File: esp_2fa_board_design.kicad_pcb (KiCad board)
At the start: 2 copper layers, 0 parts

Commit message: Started layout of components. Fixed the Edge cut of PCB and rough location of components. Routing is yet to be done
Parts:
- added BT1: 3v, BU2032SM-BT-GTR:BU2032SMBTGTR, B.Cu at (108.7, 110.8)
- added Brd1: SSD1306, SSD1306:128x64OLED, F.Cu at (132.0, 92.7)
- added C3: 1uF, Capacitor_SMD:C_1206_3216Metric, F.Cu at (167.7, 91.2)
- added C4: 10uF, Capacitor_SMD:C_1206_3216Metric, F.Cu at (144.8, 97.5)
- added C5: 1uF, Capacitor_SMD:C_1206_3216Metric, F.Cu at (114.3, 118.8)
- added C6: 10uF, Capacitor_SMD:C_1206_3216Metric, F.Cu at (153.2, 114.4)
- added C7: 0.1uF, Capacitor_SMD:C_1206_3216Metric, F.Cu at (157.9, 117.6)
- added C8: 10uF, Capacitor_SMD:C_1206_3216Metric, F.Cu at (162.1, 114.4)
- added C9: 10uF, Capacitor_SMD:C_1206_3216Metric, F.Cu at (165.8, 114.4)
- added D2: LED, LED_SMD:LED_0603_1608Metric_Castellated, F.Cu at (149.5, 93.7)
- added D3: 1N5819, Diode_SMD:D_SOD-123, F.Cu at (162.0, 95.2)
- added IC1: TPS22919DCKR, TPS22919DCKR:SOT65P210X110-6N, F.Cu at (109.6, 119.5)
- added J1: Conn_01x06_Female, Connector_PinHeader_2.00mm:PinHeader_1x06_P2.00mm_Vertical, F.Cu at (119.6, 119.0)
- added J2: TYPE-C-31-M-17, TYPE-C-31-M-17:TYPEC31M17, F.Cu at (152.8, 84.4)
- added L1: 2.2 uH, CDRH104RNP-150NC:INDPM102100X400N, F.Cu at (157.2, 106.7)
- added Q1: DMP2305U-7, DMP2305U-7:SOT96P240X110-3N, F.Cu at (158.4, 94.8)
- added R1: 100, Resistor_SMD:R_0603_1608Metric, F.Cu at (161.9, 117.6)
- added R10: 100k, Resistor_SMD:R_0603_1608Metric, F.Cu at (168.0, 95.3)
- added R11: 5.1k, Resistor_SMD:R_0603_1608Metric, F.Cu at (149.1, 90.5)
- added R12: 5.1k, Resistor_SMD:R_0603_1608Metric, F.Cu at (156.4, 90.5)
- added R13: 10k, Resistor_SMD:R_0603_1608Metric, F.Cu at (155.6, 94.7)
- added R14: 10k, Resistor_SMD:R_0603_1608Metric, F.Cu at (119.8, 114.6)
- added R2: 4.7k, Resistor_SMD:R_0603_1608Metric, F.Cu at (105.6, 110.0)
- added R3: 4.7k, Resistor_SMD:R_0603_1608Metric, F.Cu at (105.6, 119.0)
- added R4: 10k, Resistor_SMD:R_0603_1608Metric, F.Cu at (119.8, 111.1)
- added R5: 10k, Resistor_SMD:R_0603_1608Metric, F.Cu at (161.5, 90.7)
- added R6: 10k, Resistor_SMD:R_0603_1608Metric, F.Cu at (134.2, 111.0)
- added R7: 4.7k, Resistor_SMD:R_0603_1608Metric, F.Cu at (149.3, 95.2)
- added R8: 1k, Resistor_SMD:R_0603_1608Metric, F.Cu at (146.9, 94.5)
- added R9: 100k, Resistor_SMD:R_0603_1608Metric, F.Cu at (166.0, 95.3)
- added REF**: OSHW-Logo_19x20mm_SilkScreen, Symbol:OSHW-Logo_19x20mm_SilkScreen, B.Cu at (125.9, 92.5)
- added REF**: KiCad-Logo2_5mm_SilkScreen, Symbol:KiCad-Logo2_5mm_SilkScreen, B.Cu at (141.3, 86.6)
- added SW1: SW_Push, Button_Switch_SMD:SW_Push_1P1T_NO_6x6mm_H9.5mm, F.Cu at (113.3, 112.8)
- added SW2: SW_Push, Button_Switch_SMD:SW_Push_1P1T_NO_6x6mm_H9.5mm, F.Cu at (127.0, 112.8)
- added SW3: BOOT, Button_Switch_SMD:SW_Push_1P1T_NO_6x6mm_H9.5mm, F.Cu at (140.3, 112.8)
- added SW4: RESET, Button_Switch_SMD:SW_Push_1P1T_NO_6x6mm_H9.5mm, F.Cu at (165.1, 85.2)
- added U1: ESP32-WROOM-32, RF_Module:ESP32-WROOM-32, F.Cu at (102.1, 95.9)
- added U2: DS3231M, Package_SO:SOIC-16W_7.5x10.3mm_P1.27mm, F.Cu at (97.7, 114.5)
- added U3: MCP73831-2-OT, Package_TO_SOT_SMD:SOT-23-5, F.Cu at (148.0, 97.9)
- added U4: TPS63001, Package_SON:Texas_DRC0010J_ThermalVias, F.Cu at (157.6, 114.3)
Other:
- board outline added: 82 x 45 mm

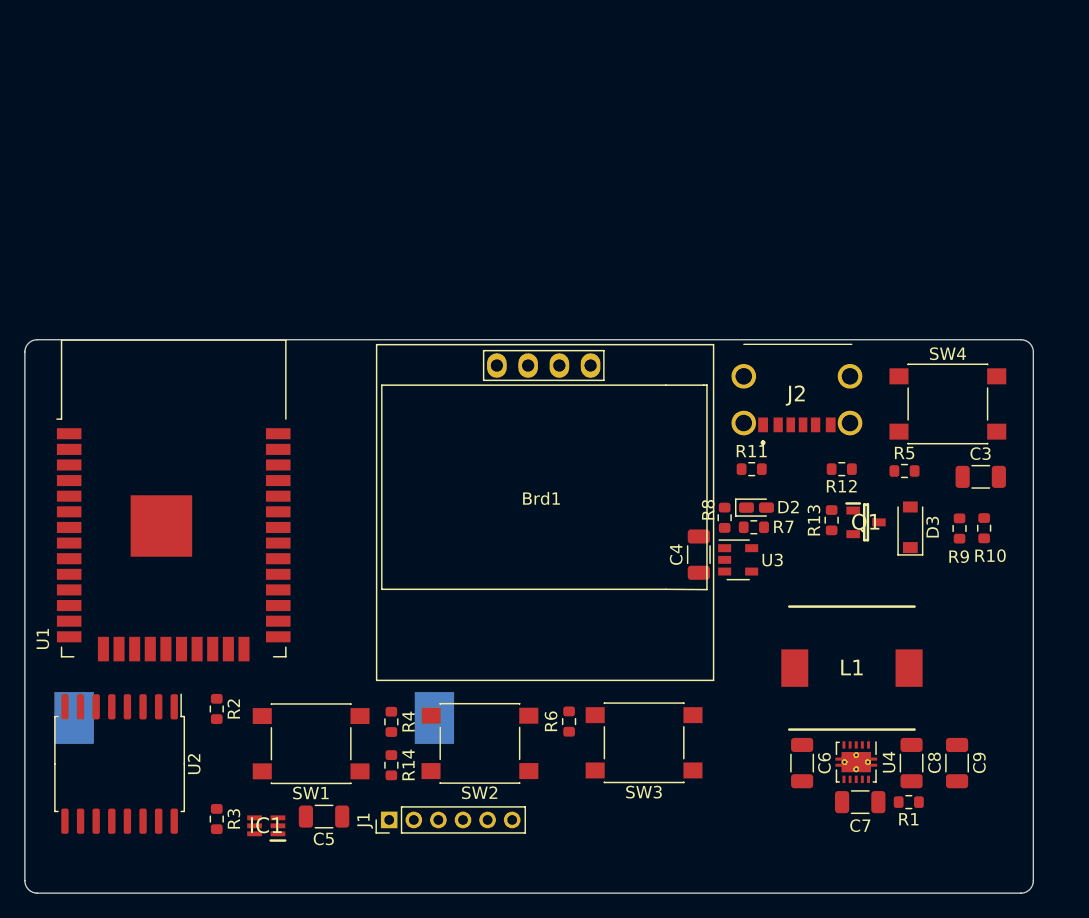
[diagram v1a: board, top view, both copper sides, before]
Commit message: Partially completed routing
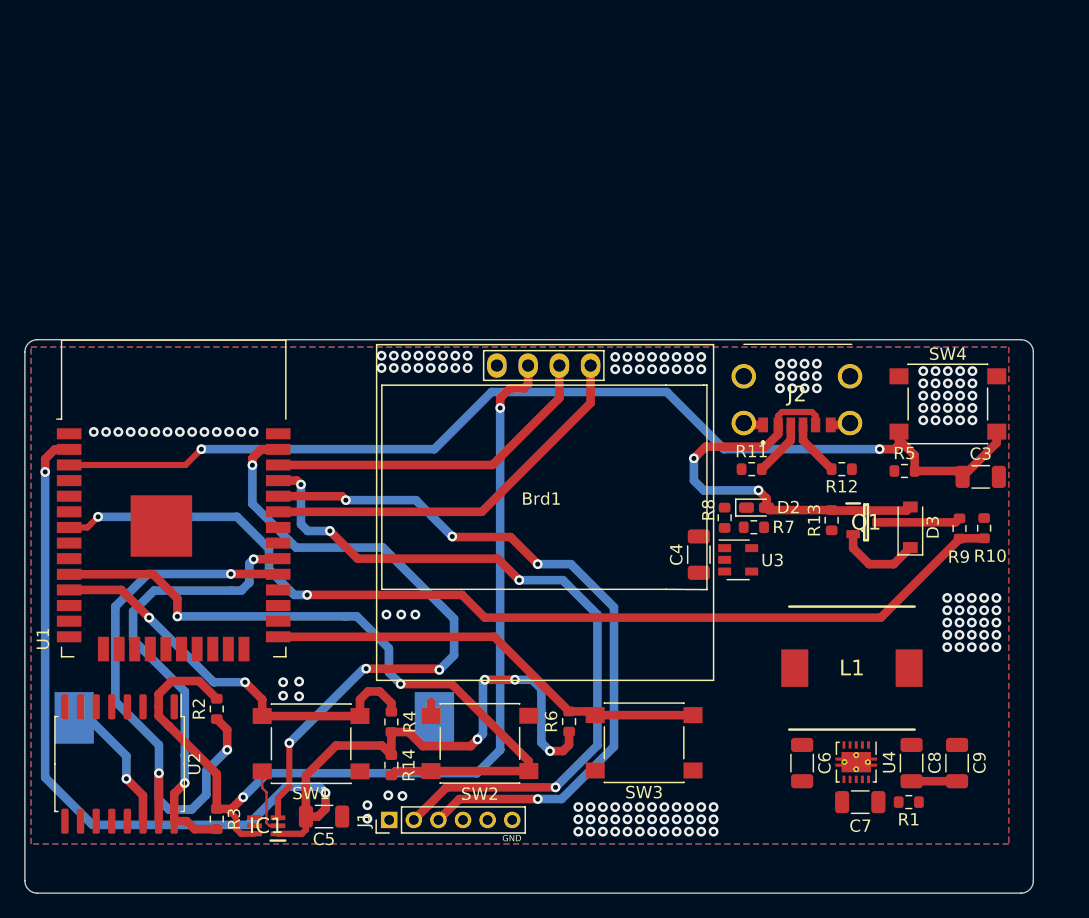
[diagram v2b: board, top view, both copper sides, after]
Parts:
- turned BT1 to 180 degrees
- turned R2 to 270 degrees
- turned R4 to 90 degrees
- turned SW2 to 0 degrees
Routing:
- net +3V3: track 0.00 -> 104.1 mm, vias 0 -> 6
- net /EN: track 0.00 -> 85.7 mm, vias 0 -> 2
- net /A1_7_BATT: track 0.00 -> 81.8 mm, vias 0 -> 2
- net /LOAD_SWITCH_VCC: track 0.00 -> 79.4 mm, vias 0 -> 2
- net /TX: track 0.00 -> 60.4 mm, vias 0 -> 4
- net /RX: track 0.00 -> 59.1 mm, vias 0 -> 4
- net /IO25: track 0.00 -> 57.8 mm, vias 0 -> 2
- net /IO23: track 0.00 -> 52.2 mm, vias 0 -> 4
- net /IO5_SDA: track 0.00 -> 47.3 mm, vias 0 -> 3
- net /IO18_SCL: track 0.00 -> 37.4 mm, vias 0 -> 2
- net /BOOT: track 0.00 -> 36.4 mm
- net VBUS: track 0.00 -> 34.2 mm, vias 0 -> 2
- net /IO26: track 0.00 -> 34.0 mm, vias 0 -> 2
- net /IO21_SDA: track 0.00 -> 32.1 mm
- net /IO22_SCL: track 0.00 -> 27.8 mm
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- added copper zone on B.Cu, net GND
- added copper zone on F.Cu, net GND
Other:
- net class Default: clearance 0.000254 -> 0.2; trace_width 0.000254 -> 0.2; via_dia 0.000762 -> 0.8; via_drill 0.000381 -> 0.4
- rule trace_clearance: 0.000254 -> 0.2
- board text added: "GND"

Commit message: Addede datasheets and partially completed routing
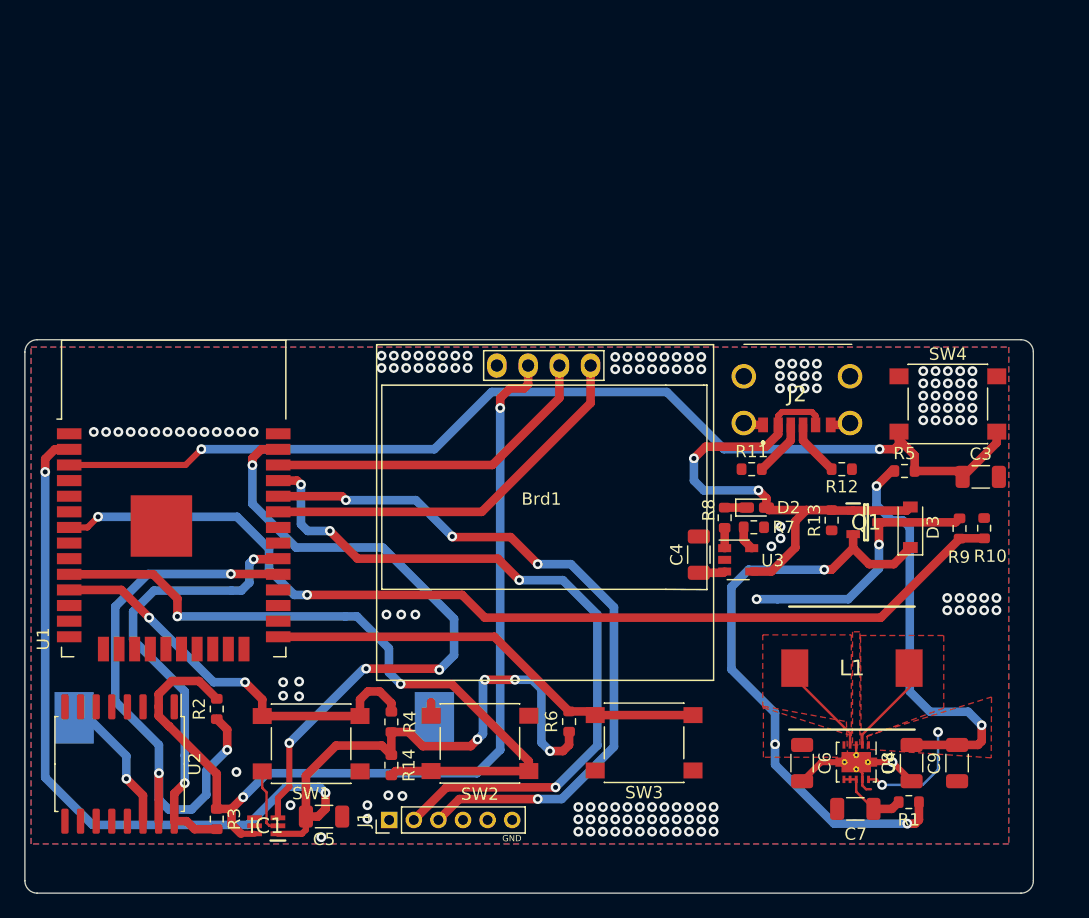
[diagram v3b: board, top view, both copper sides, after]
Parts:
- moved C7 0.68 mm to (157.5, 118.2), turned to 180 degrees
- turned C8 to 270 degrees
- turned C9 to 270 degrees
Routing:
- net /V_INPUT: track 6.89 -> 49.3 mm, vias 0 -> 3
- net +3V3: track 104.1 -> 144.2 mm, vias 6 -> 10
- net +BATT: track 6.68 -> 23.6 mm, vias 0 -> 2
- net GND: track 9.81 -> 21.4 mm, vias 155 -> 147
- net Net-(L1-Pad1): track 0.00 -> 8.11 mm
- net Net-(L1-Pad2): track 0.00 -> 7.82 mm
- net VBUS: track 34.2 -> 42.0 mm
- net Net-(C7-Pad1): track 0.00 -> 6.26 mm
- net Net-(R7-Pad1): track 0.00 -> 1.97 mm
- net Net-(D2-Pad1): track 0.00 -> 1.78 mm
- net Net-(R8-Pad1): track 0.00 -> 1.65 mm
- added copper zone on F.Cu, net +3V3
- added copper zone on F.Cu, net /V_INPUT
- added copper zone on F.Cu, net Net-(L1-Pad1)
- added copper zone on F.Cu, net Net-(L1-Pad2)

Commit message: Completed PCB routing
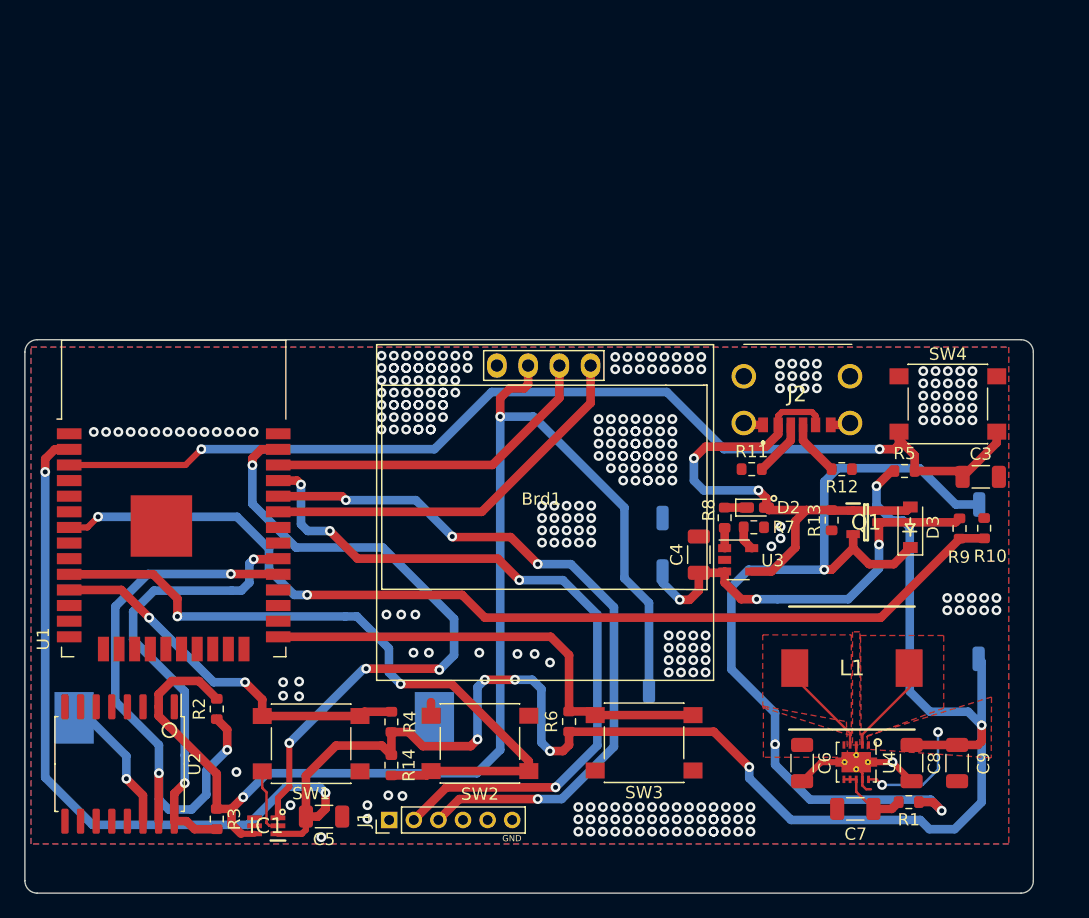
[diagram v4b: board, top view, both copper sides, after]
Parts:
- added +BATT: +BATT, Connector_Wire:SolderWirePad_1x01_SMD_1x2mm, B.Cu at (141.8, 98.8)
- added GND: GND, Connector_Wire:SolderWirePad_1x01_SMD_1x2mm, B.Cu at (141.8, 94.5)
- added TP1: 3V3, Connector_Wire:SolderWirePad_1x01_SMD_1x2mm, B.Cu at (167.6, 106.0)
- added TP4: LOAD_SWITCH, Connector_Wire:SolderWirePad_1x01_SMD_1x2mm, B.Cu at (140.8, 108.5)
- added TP5: V_INPUT, Connector_Wire:SolderWirePad_1x01_SMD_1x2mm, B.Cu at (167.6, 93.4)
- moved REF** 1.39 mm to (140.1, 87.2)
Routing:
- net +3V3: track 144.2 -> 194.2 mm, vias 10 -> 11
- net /LOAD_SWITCH_VCC: track 79.3 -> 108.2 mm
- net /V_INPUT: track 49.3 -> 72.7 mm
- net +BATT: track 23.6 -> 33.8 mm, vias 2 -> 3
- net /BOOT: track 36.4 -> 39.0 mm
- net /IO26: track 34.0 -> 31.4 mm
- net GND: vias 147 -> 289
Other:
- board text added: "Open Authenticator"
- board text added: "v1.2 Vedant Paranjape"

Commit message: Updated schematics according review feedback
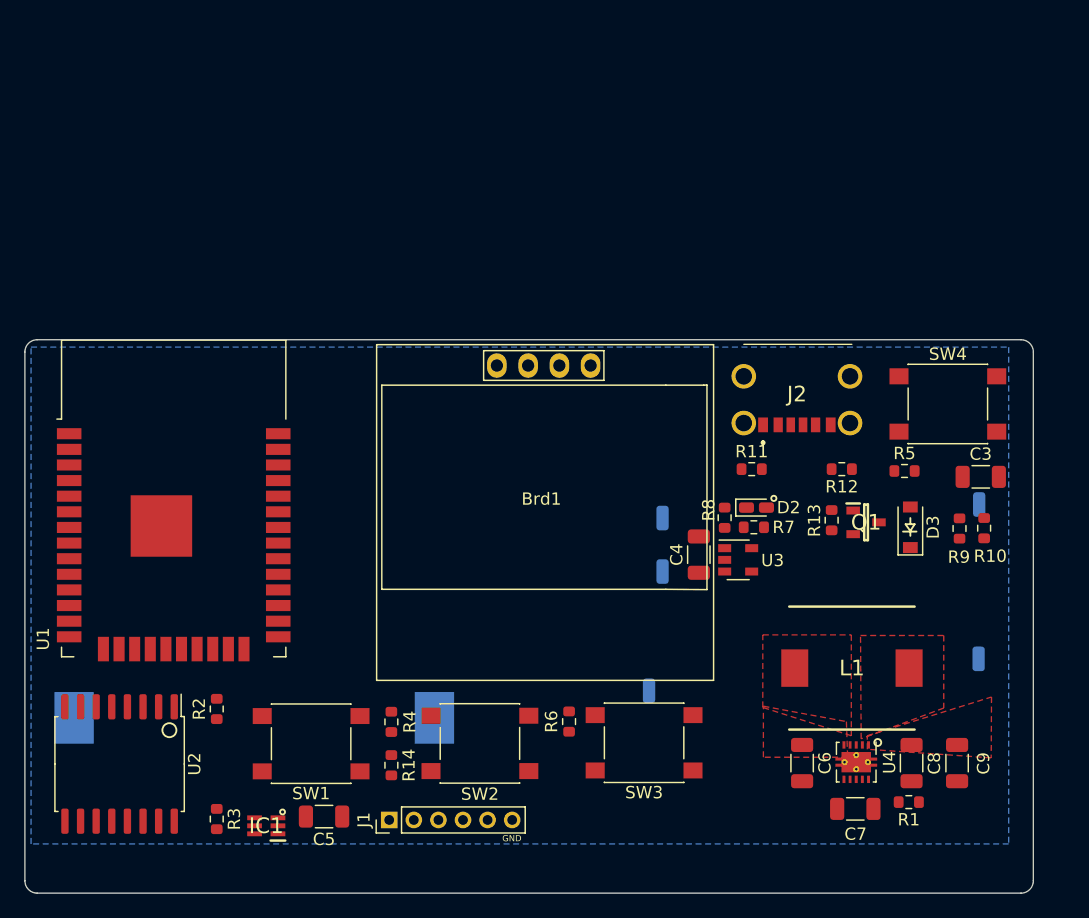
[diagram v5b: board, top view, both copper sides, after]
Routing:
- net +3V3: track 194.2 -> 0.00 mm, vias 11 -> 0
- net /LOAD_SWITCH_VCC: track 108.2 -> 0.00 mm, vias 2 -> 0
- net /EN: track 85.7 -> 0.00 mm, vias 2 -> 0
- net /A1_7_BATT: track 81.8 -> 0.00 mm, vias 2 -> 0
- net /V_INPUT: track 72.7 -> 0.00 mm, vias 3 -> 0
- net /TX: track 60.4 -> 0.00 mm, vias 4 -> 0
- net /RX: track 59.1 -> 0.00 mm, vias 4 -> 0
- net /IO25: track 57.8 -> 0.00 mm, vias 2 -> 0
- net /IO23: track 52.2 -> 0.00 mm, vias 4 -> 0
- net /IO5_SDA: track 47.3 -> 0.00 mm, vias 3 -> 0
- net VBUS: track 42.0 -> 0.00 mm, vias 2 -> 0
- net /BOOT: track 39.0 -> 0.00 mm
- net /IO18_SCL: track 37.4 -> 0.00 mm, vias 2 -> 0
- net +BATT: track 33.8 -> 0.00 mm, vias 3 -> 0
- net /IO21_SDA: track 32.1 -> 0.00 mm
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- removed copper zone on F.Cu, net GND

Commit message: Partially completed rerouting
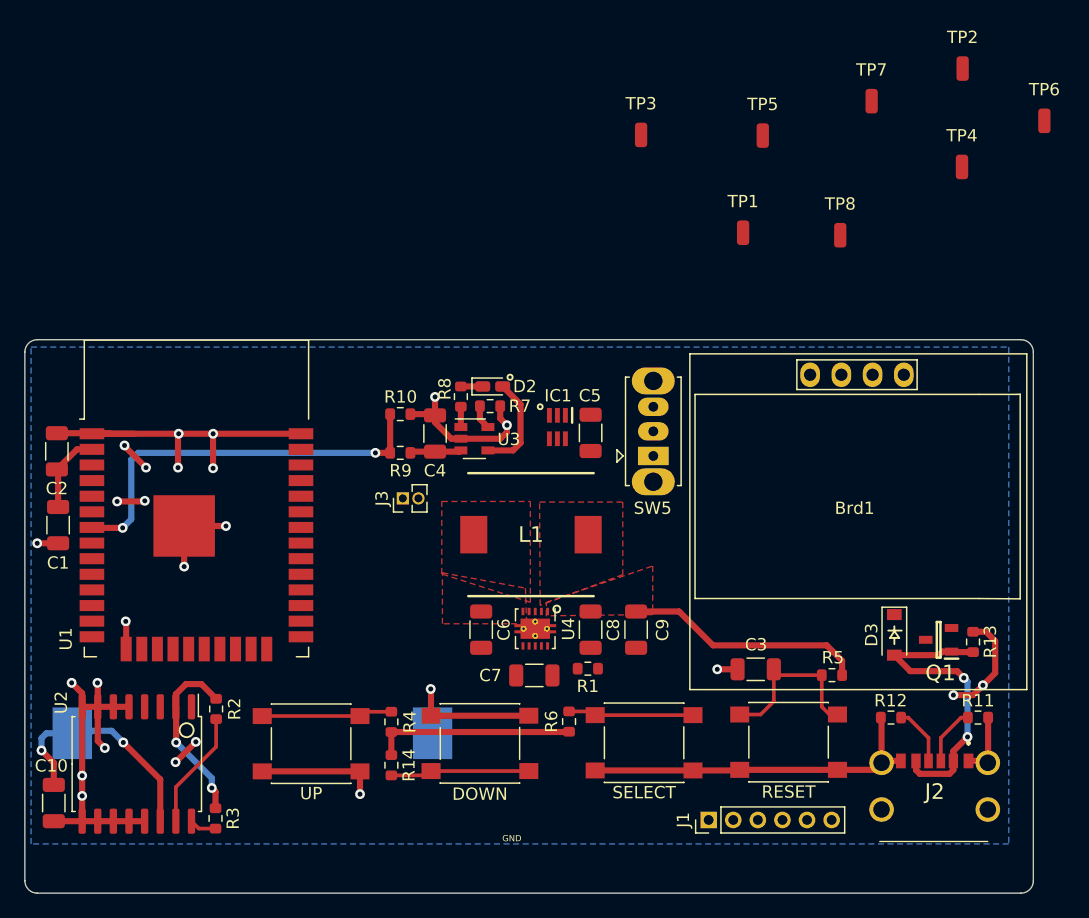
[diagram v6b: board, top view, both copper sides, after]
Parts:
- removed +BATT: +BATT, Connector_Wire:SolderWirePad_1x01_SMD_1x2mm
- removed GND: GND, Connector_Wire:SolderWirePad_1x01_SMD_1x2mm
- removed SW4: RESET, Button_Switch_SMD:SW_Push_1P1T_NO_6x6mm_H9.5mm
- added C1: 10uF 50V, Capacitor_SMD:C_1206_3216Metric, F.Cu at (92.7, 95.1)
- added C10: 1uF 50V, Capacitor_SMD:C_1206_3216Metric, F.Cu at (92.3, 117.7)
- added C2: 0.1uF 50V, Capacitor_SMD:C_1206_3216Metric, F.Cu at (92.6, 89.1)
- added J3: Conn_01x02_Female, Connector_PinHeader_1.27mm:PinHeader_1x02_P1.27mm_Vertical, F.Cu at (120.7, 92.9)
- added RESET: RESET, Button_Switch_SMD:SW_Push_1P1T_NO_6x6mm_H9.5mm, F.Cu at (152.1, 112.7)
- added SW5: POWER SWITCH, Button_Switch_THT:SW_Slide_1P2T_CK_OS102011MS2Q, F.Cu at (141.1, 89.5)
- added TP2: RTC_SDA, Connector_Wire:SolderWirePad_1x01_SMD_1x2mm, F.Cu at (166.2, 58.0)
- added TP3: RTC_SCL, Connector_Wire:SolderWirePad_1x01_SMD_1x2mm, F.Cu at (140.1, 63.3)
- added TP6: OLED_SDA, Connector_Wire:SolderWirePad_1x01_SMD_1x2mm, F.Cu at (172.9, 62.2)
- added TP7: OLED_SCL, Connector_Wire:SolderWirePad_1x01_SMD_1x2mm, F.Cu at (158.8, 60.6)
- added TP8: GND, Connector_Wire:SolderWirePad_1x01_SMD_1x2mm, F.Cu at (156.3, 71.5)
- C3, C5: value 1uF -> 1uF 50V
- C4, C6, C8, C9: value 10uF -> 10uF 50V
- C7: value 0.1uF -> 0.1uF 50V
- TP1, TP4, TP5: moved to F.Cu
- moved TP4 49.6 mm to (166.2, 66.0)
- moved R10 48.4 mm to (120.5, 86.0), turned to 0 degrees
- moved R9 45.9 mm to (120.5, 89.2), turned to 180 degrees
- moved IC1 40.1 mm to (133.3, 87.1), turned to 270 degrees
- moved TP1 39.6 mm to (148.4, 71.3)
- moved C5 38.0 mm to (136.0, 87.6), turned to 90 degrees
- moved REF** 36.8 mm to (120.4, 56.1)
- moved TP5 34.8 mm to (150.0, 63.4)
- moved J2 34.2 mm to (164.0, 116.8), turned to 0 degrees
- moved C9 28.3 mm to (139.7, 103.6)
- moved C7 28.3 mm to (131.4, 107.3)
- moved L1 28.3 mm to (131.2, 95.8)
- moved C6 28.3 mm to (127.1, 103.6)
- moved C8 28.3 mm to (136.0, 103.6)
- moved R1 28.3 mm to (135.8, 106.8)
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- renumbered SW2 to DOWN, SW3 to SELECT, SW1 to UP
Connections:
- C6 pad 1: /V_INPUT -> Net-(C6-Pad1)
- R1 pad 1: /V_INPUT -> Net-(C6-Pad1)
- U4 pad 5: /V_INPUT -> Net-(C6-Pad1)
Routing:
- net GND: track 0.00 -> 156.2 mm, vias 0 -> 26
- net +3V3: track 0.00 -> 42.5 mm
- net VBUS: track 0.00 -> 33.2 mm, vias 0 -> 2
- net /A1_7_BATT: track 0.00 -> 32.8 mm, vias 0 -> 2
- net Net-(BT1-Pad1): track 0.00 -> 17.8 mm, vias 0 -> 2
- net /LOAD_SWITCH_VCC: track 0.00 -> 14.7 mm, vias 0 -> 2
- net /EN: track 0.00 -> 14.0 mm
- net /IO25: track 0.00 -> 11.3 mm
- net /IO26: track 0.00 -> 10.6 mm
- net /BOOT: track 0.00 -> 10.2 mm
- net /IO5_SDA: track 0.00 -> 9.66 mm
- net Net-(J2-PadA5): track 0.00 -> 4.79 mm
- net Net-(J2-PadB5): track 0.00 -> 4.76 mm
- net +BATT: track 0.00 -> 4.18 mm
- net /IO18_SCL: track 0.00 -> 2.20 mm
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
